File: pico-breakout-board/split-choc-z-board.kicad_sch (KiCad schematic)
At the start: 79 parts, among them J1 USB4105-GF-A, J2 USB4105-GF-A, J3 Conn_01x04_Pin, J4 Conn_01x02, SW1 SW_SPST, SW10 SW_SPST, SW11 SW_SPST, SW12 SW_SPST, SW13 SW_SPST, SW14 SW_SPST, SW15 SW_SPST, SW16 SW_SPST, SW17 SW_SPST, SW18 SW_SPST, SW19 SW_SPST, SW2 SW_SPST, SW20 SW_SPST, SW21 SW_SPST, SW22 SW_SPST, SW3 SW_SPST, SW4 SW_SPST, SW5 SW_SPST, SW6 SW_SPST, SW7 SW_SPST, SW8 SW_SPST, SW9 SW_SPST, U2 RP2040, U3 NCP1117-3.3_SOT223, U4 W25Q128JVS, U5 USBLC6-2SC6, X1 ABM8-272-T3

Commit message: Removed matrix and added 2.54mm pins 2x20
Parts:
- removed D1, D10, D11, D12, D13, D14, D15, D16, D17, D18, D19, D2, D20, D3, D4, D5, D6, D7, D8, D9: D, footprints:SOD123_MCC, symbol Device:D
- removed GND1, GP24, GP25: TestPoint, TestPoint:TestPoint_Pad_D2.0mm, symbol Connector:TestPoint
- removed J4: Conn_01x02, Connector_PinHeader_2.54mm:PinHeader_1x02_P2.54mm_Vertical, symbol Connector_Generic:Conn_01x02
- removed SW1, SW10, SW11, SW12, SW13, SW14, SW15, SW16, SW17, SW18, SW19, SW2, SW20, SW3, SW4, SW5, SW6, SW7, SW8, SW9: SW_SPST, ScottoKeebs_Choc:Choc_V1_1.00u, symbol Switch:SW_SPST
- added J5: Conn_02x20_Counter_Clockwise, Connector_PinHeader_2.54mm:PinHeader_2x20_P2.54mm_Vertical, symbol Connector_Generic:Conn_02x20_Counter_Clockwise
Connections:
- net +3V3: now also J5.25 (Pin_25), J5.26 (Pin_26), J5.27 (Pin_27), J5.28 (Pin_28); no longer U2.2 (GPIO0)
- net B-B_D+: no longer U2.13 (GPIO10)
- net B-B_D-: no longer U2.14 (GPIO11)
- net DEBUG_CLK: now also J5.39 (Pin_39)
- net DEBUG_DATA: now also J5.40 (Pin_40)
- net GND: now also J5.21 (Pin_21), J5.22 (Pin_22), J5.23 (Pin_23), J5.24 (Pin_24)
- net GPIO12: now reaches U2.15 (GPIO12)
- net GPIO12: now also J5.8 (Pin_8)
- net GPIO13: now reaches U2.16 (GPIO13)
- net GPIO13: now also J5.7 (Pin_7)
- net GPIO14: now reaches U2.17 (GPIO14)
- net GPIO14: now also J5.6 (Pin_6)
- net GPIO15: now reaches U2.18 (GPIO15)
- net GPIO15: now also J5.5 (Pin_5)
- net GPIO16: now reaches U2.27 (GPIO16)
- net GPIO16: now also J5.4 (Pin_4)
- net GPIO17: now reaches U2.28 (GPIO17)
- net GPIO17: now also J5.3 (Pin_3)
- net GPIO18: now reaches U2.29 (GPIO18)
- net GPIO18: now also J5.2 (Pin_2)
- net GPIO19: now reaches U2.30 (GPIO19)
- net GPIO19: now also J5.1 (Pin_1)
- net GPIO20: now reaches U2.31 (GPIO20)
- net GPIO20: now also J5.38 (Pin_38)
- net GPIO21: now reaches U2.32 (GPIO21)
- net GPIO21: now also J5.37 (Pin_37)
- net GPIO22: now reaches U2.34 (GPIO22)
- net GPIO22: now also J5.36 (Pin_36)
- net GPIO23: now reaches U2.35 (GPIO23)
- net GPIO23: now also J5.35 (Pin_35)
- net GPIO26: now reaches U2.38 (GPIO26_ADC0)
- net GPIO26: now also J5.32 (Pin_32)
- net GPIO27: now reaches U2.39 (GPIO27_ADC1)
- net GPIO27: now also J5.31 (Pin_31)
- net GPIO28: now reaches U2.40 (GPIO28_ADC2)
- net GPIO28: now also J5.30 (Pin_30)
- net GPIO29: now reaches U2.41 (GPIO29_ADC3)
- net GPIO29: now also J5.29 (Pin_29)
- net Col_1 renamed GPIO1
- net GPIO1: now also J5.19 (Pin_19)
- net Col_2 renamed GPIO2
- net GPIO2: now also J5.18 (Pin_18)
- net Col_3 renamed GPIO3
- net GPIO3: now also J5.17 (Pin_17)
- net Col_4 renamed GPIO4
- net GPIO4: now also J5.16 (Pin_16)
- net GP24 renamed GPIO24
- net GPIO24: now also J5.34 (Pin_34)
- net GP25 renamed GPIO25
- net GPIO25: now also J5.33 (Pin_33)
- net Row_1 renamed GPIO5
- net GPIO5: now also J5.15 (Pin_15)
- net Row_2 renamed GPIO6
- net GPIO6: now also J5.14 (Pin_14)
- net Row_3 renamed GPIO7
- net GPIO7: now also J5.13 (Pin_13)
- net Row_4 renamed GPIO8
- net GPIO8: now also J5.12 (Pin_12)
- net Row_5 renamed GPIO9
- net GPIO9: now also J5.11 (Pin_11)
- new net GPIO0: J5.20 (Pin_20), U2.2 (GPIO0)
- new net GPIO10: J5.10 (Pin_10), U2.13 (GPIO10)
- new net GPIO11: J5.9 (Pin_9), U2.14 (GPIO11)
- no-connect marks 28 -> 12
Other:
- note removed: "Debug"
- note removed: "Keyboard matrix"
- note removed: "Use this in QMK: #define SPLIT_HAND_PIN A0 HIGH is left hand"

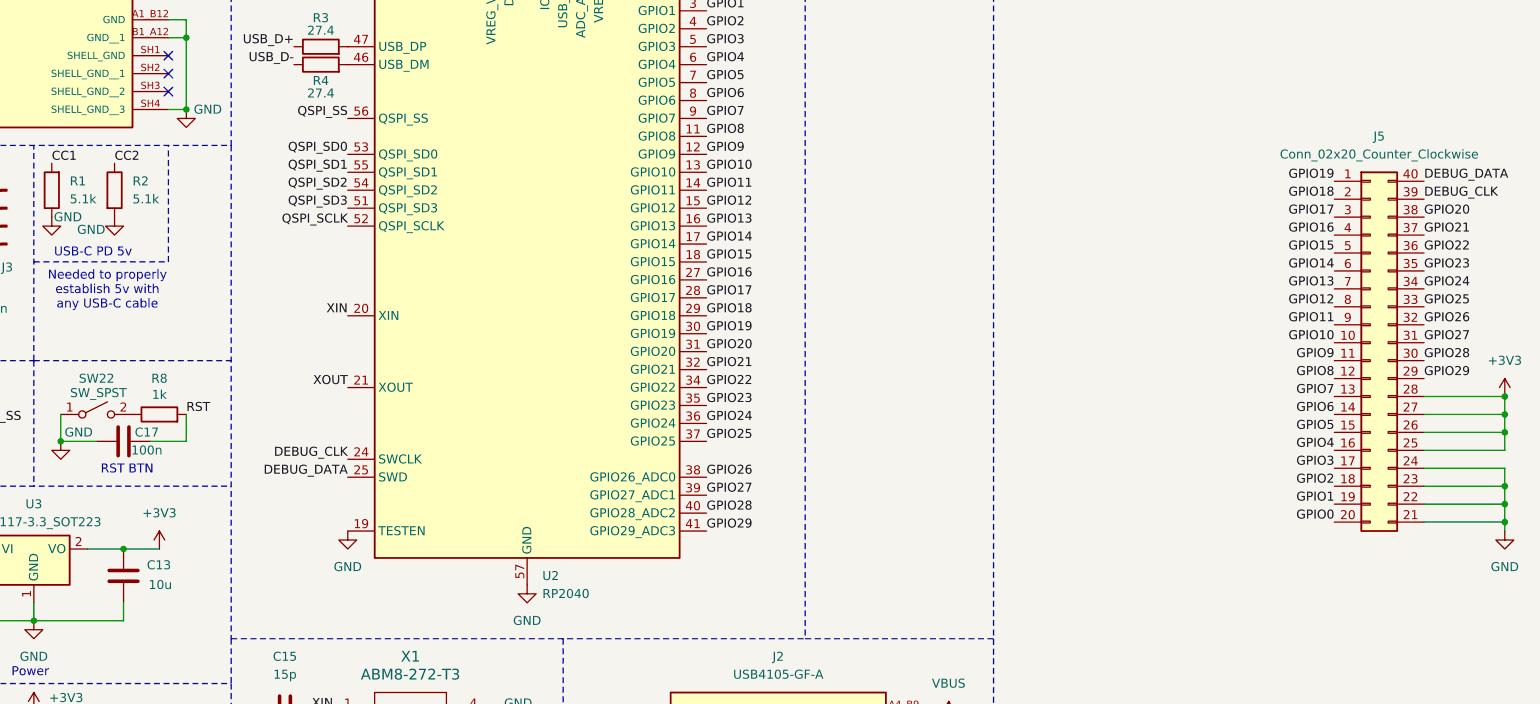
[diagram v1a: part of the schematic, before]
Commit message: Finished bare redesign
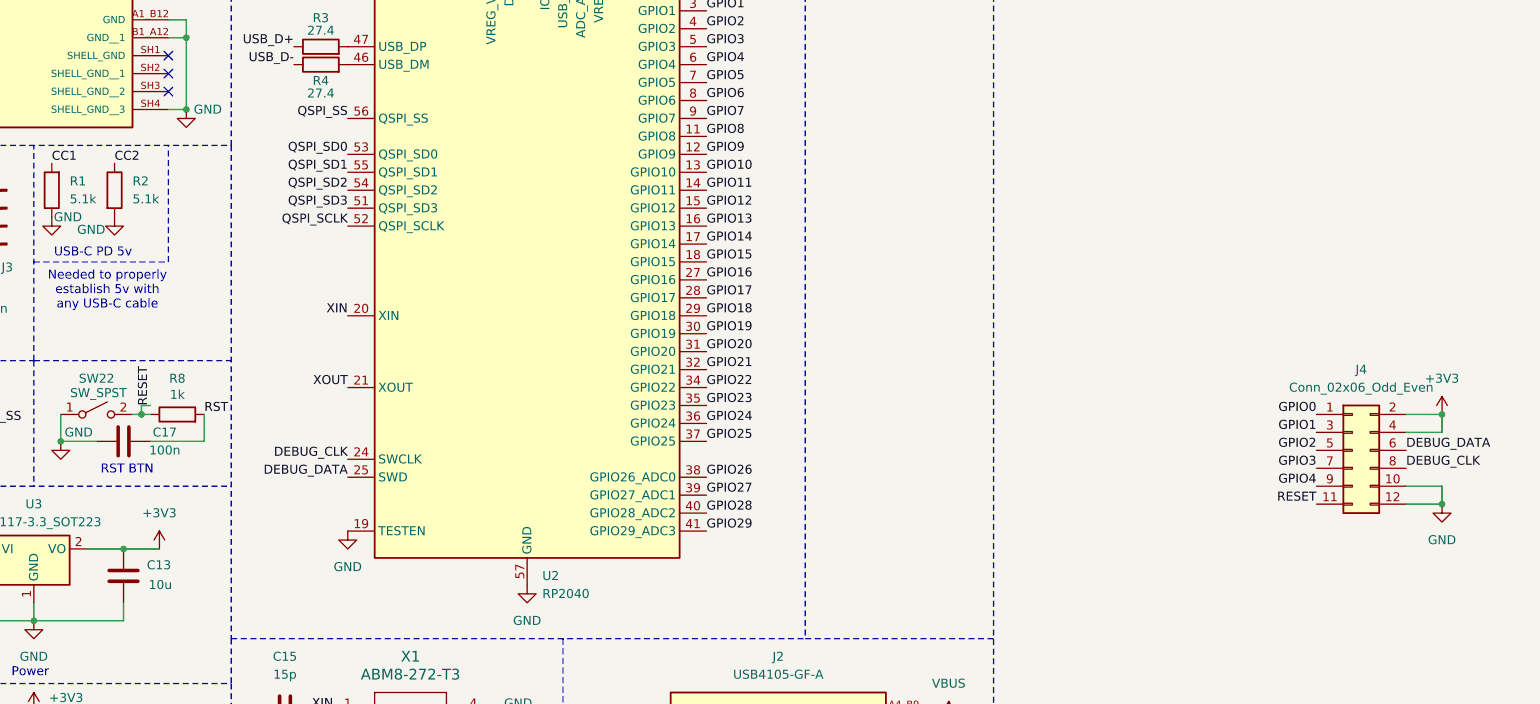
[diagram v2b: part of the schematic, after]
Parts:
- removed J5: Conn_02x20_Counter_Clockwise, Connector_PinHeader_2.54mm:PinHeader_2x20_P2.54mm_Vertical, symbol Connector_Generic:Conn_02x20_Counter_Clockwise
- added J4: Conn_02x06_Odd_Even, Connector_PinSocket_2.54mm:PinSocket_2x06_P2.54mm_Vertical, symbol Connector_Generic:Conn_02x06_Odd_Even
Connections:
- net +3V3: now also J4.2 (Pin_2), J4.4 (Pin_4)
- net DEBUG_CLK: now also J4.8 (Pin_8)
- net DEBUG_DATA: now also J4.6 (Pin_6)
- net GND: now also J4.10 (Pin_10), J4.12 (Pin_12)
- net GPIO0: now also J4.1 (Pin_1)
- net GPIO1: now also J4.3 (Pin_3)
- net GPIO2: now also J4.5 (Pin_5)
- net GPIO3: now also J4.7 (Pin_7)
- net GPIO4: now also J4.9 (Pin_9)
- net RESET: now reaches R8.1, SW22.2 (B)
- net RESET: now also J4.11 (Pin_11)
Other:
- moved on the sheet: R8

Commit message: Forgot no connects
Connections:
- net GPIO10 is gone; now on net B-B_D+: U2.13 (GPIO10)
- net GPIO11 is gone; now on net B-B_D-: U2.14 (GPIO11)
- net GPIO12: no longer names the net of U2.15 (GPIO12)
- net GPIO13: no longer names the net of U2.16 (GPIO13)
- net GPIO14: no longer names the net of U2.17 (GPIO14)
- net GPIO15: no longer names the net of U2.18 (GPIO15)
- net GPIO16: no longer names the net of U2.27 (GPIO16)
- net GPIO17: no longer names the net of U2.28 (GPIO17)
- net GPIO18: no longer names the net of U2.29 (GPIO18)
- net GPIO19: no longer names the net of U2.30 (GPIO19)
- net GPIO20: no longer names the net of U2.31 (GPIO20)
- net GPIO21: no longer names the net of U2.32 (GPIO21)
- net GPIO22: no longer names the net of U2.34 (GPIO22)
- net GPIO23: no longer names the net of U2.35 (GPIO23)
- net GPIO24: no longer names the net of U2.36 (GPIO24)
- net GPIO25: no longer names the net of U2.37 (GPIO25)
- net GPIO26: no longer names the net of U2.38 (GPIO26_ADC0)
- net GPIO27: no longer names the net of U2.39 (GPIO27_ADC1)
- net GPIO28: no longer names the net of U2.40 (GPIO28_ADC2)
- net GPIO29: no longer names the net of U2.41 (GPIO29_ADC3)
- net GPIO5: no longer names the net of U2.7 (GPIO5)
- net GPIO6: no longer names the net of U2.8 (GPIO6)
- net GPIO7: no longer names the net of U2.9 (GPIO7)
- net GPIO8: no longer names the net of U2.11 (GPIO8)
- net GPIO9: no longer names the net of U2.12 (GPIO9)
- no-connect marks 12 -> 35
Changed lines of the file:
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@@
+	)
+	(no_connect
+		(at 137.16 111.76)
+	)
+	(no_connect
+		(at 137.16 60.96)
+	)
+	(no_connect
+		(at 137.16 101.6)
+	)
+	(no_connect
+		(at 137.16 91.44)
 	)
 	(no_connect
@@
 	)
 	(no_connect
+		(at 137.16 83.82)
+	)
+	(no_connect
+		(at 137.16 99.06)
+	)
+	(no_connect
+		(at 137.16 114.3)
+	)
+	(no_connect
+		(at 137.16 78.74)
+	)
+	(no_connect
 		(at 60.96 49.53)
 	)
@@
 	)
 	(no_connect
+		(at 137.16 106.68)
+	)
+	(no_connect
 		(at 167.64 167.64)
 	)
@@
 	)
 	(no_connect
+		(at 137.16 86.36)
+	)
+	(no_connect
 		(at 167.64 170.18)
 	)
@@
 	)
 	(no_connect
+		(at 137.16 93.98)
+	)
+	(no_connect
 		(at 60.96 52.07)
 	)
 	(no_connect
+		(at 137.16 88.9)
+	)
+	(no_connect
+		(at 137.16 81.28)
+	)
+	(no_connect
+		(at 137.16 68.58)
+	)
+	(no_connect
+		(at 137.16 58.42)
+	)
+	(no_connect
+		(at 137.16 55.88)
+	)
+	(no_connect
+		(at 137.16 50.8)
+	)
+	(no_connect
+		(at 137.16 109.22)
+	)
+	(no_connect
+		(at 137.16 71.12)
+	)
+	(no_connect
+		(at 137.16 53.34)
+	)
+	(no_connect
+		(at 137.16 96.52)
+	)
+	(no_connect
+		(at 137.16 76.2)
+	)
+	(no_connect
 		(at 127 144.78)
 	)
@@
 	(no_connect
 		(at 167.64 154.94)
+	)
+	(no_connect
+		(at 137.16 73.66)
 	)
 	(wire
@@
 		)
 	)
-	(label "GPIO12"
-		(at 137.16 68.58 0)
+	(label "B-B_D+"
+		(at 137.16 63.5 0)
+		(effects
+			(font
+				(size 1.27 1.27)
+			)
+			(justify left bottom)
+		)
+	)
+	(label "B-B_D-"
+		(at 137.16 66.04 0)
 		(effects
 			(font
@@
 		)
 	)
-	(label "GPIO23"
-		(at 137.16 96.52 0)
-		(effects
-			(font
-				(size 1.27 1.27)
-			)
-			(justify left bottom)
-		)
-	)
 	(label "DEBUG_CLK"
 		(at 86.36 104.14 180)
@@
 		)
 	)
-	(label "GPIO6"
-		(at 137.16 53.34 0)
-		(effects
-			(font
-				(size 1.27 1.27)
-			)
-			(justify left bottom)
-		)
-	)
 	(label "GPIO1"
 		(at 137.16 40.64 0)
@@
 		)
 	)
-	(label "GPIO17"
-		(at 137.16 81.28 0)
-		(effects
-			(font
-				(size 1.27 1.27)
-			)
-			(justify left bottom)
-		)
-	)
 	(label "QSPI_SD1"
 		(at 31.75 154.94 180)
@@
 		)
 	)
-	(label "GPIO7"
-		(at 137.16 55.88 0)
-		(effects
-			(font
-				(size 1.27 1.27)
-			)
-			(justify left bottom)
-		)
-	)
 	(label "USB_D+"
 		(at 20.32 29.21 180)
@@
 		)
 	)
-	(label "GPIO25"
-		(at 137.16 101.6 0)
-		(effects
-			(font
-				(size 1.27 1.27)
-			)
-			(justify left bottom)
-		)
-	)
 	(label "USB_D-"
 		(at 20.32 31.75 180)
@@
 		)
 	)
-	(label "GPIO24"
-		(at 137.16 99.06 0)
-		(effects
-			(font
-				(size 1.27 1.27)
-			)
-			(justify left bottom)
-		)
-	)
-	(label "GPIO11"
-		(at 137.16 66.04 0)
-		(effects
-			(font
-				(size 1.27 1.27)
-			)
-			(justify left bottom)
-		)
-	)
-	(label "GPIO28"
-		(at 137.16 111.76 0)
-		(effects
-			(font
-				(size 1.27 1.27)
-			)
-			(justify left bottom)
-		)
-	)
 	(label "RESET"
 		(at 58.42 96.52 90)
@@
 		)
 	)
-	(label "GPIO8"
-		(at 137.16 58.42 0)
-		(effects
-			(font
-				(size 1.27 1.27)
-			)
-			(justify left bottom)
-		)
-	)
-	(label "GPIO14"
-		(at 137.16 73.66 0)
-		(effects
-			(font
-				(size 1.27 1.27)
-			)
-			(justify left bottom)
-		)
-	)
 	(label "GPIO3"
 		(at 223.52 105.41 180)
@@
 		)
 	)
-	(label "GPIO9"
-		(at 137.16 60.96 0)
-		(effects
-			(font
-				(size 1.27 1.27)
-			)
-			(justify left bottom)
-		)
-	)
 	(label "B-B_D-"
 		(at 127 149.86 180)
@@
 		)
 	)
-	(label "GPIO13"
-		(at 137.16 71.12 0)
-		(effects
-			(font
-				(size 1.27 1.27)
-			)
-			(justify left bottom)
-		)
-	)
 	(label "QSPI_SD1"
 		(at 86.36 63.5 180)
@@
 		)
 	)
-	(label "GPIO22"
-		(at 137.16 93.98 0)
-		(effects
-			(font
-				(size 1.27 1.27)
-			)
-			(justify left bottom)
-		)
-	)
 	(label "QSPI_SCLK"
 		(at 86.36 71.12 180)
@@
 		)
 	)
-	(label "GPIO18"
-		(at 137.16 83.82 0)
-		(effects
-			(font
-				(size 1.27 1.27)
-			)
-			(justify left bottom)
-		)
-	)
 	(label "DEBUG_CLK"
 		(at 236.22 105.41 0)
@@
 		)
 	)
-	(label "GPIO20"
-		(at 137.16 88.9 0)
-		(effects
-			(font
-				(size 1.27 1.27)
-			)
-			(justify left bottom)
-		)
-	)
 	(label "QSPI_SS"
 		(at 33.02 99.06 0)
@@
 		)
 	)
-	(label "GPIO21"
-		(at 137.16 91.44 0)
-		(effects
-			(font
-				(size 1.27 1.27)
-			)
-			(justify left bottom)
-		)
-	)
 	(label "DEBUG_CLK"
 		(at 31.75 66.04 180)
@@
 		)
 	)
-	(label "GPIO27"
-		(at 137.16 109.22 0)
-		(effects
-			(font
-				(size 1.27 1.27)
-			)
-			(justify left bottom)
-		)
-	)
 	(label "B-B_D+"
 		(at 107.95 168.91 270)
@@
 		)
 	)
-	(label "GPIO5"
-		(at 137.16 50.8 0)
-		(effects
-			(font
-				(size 1.27 1.27)
-			)
-			(justify left bottom)
-		)
-	)
-	(label "GPIO10"
-		(at 137.16 63.5 0)
-		(effects
-			(font
-				(size 1.27 1.27)
-			)
-			(justify left bottom)
-		)
-	)
-	(label "GPIO19"
-		(at 137.16 86.36 0)
-		(effects
-			(font
-				(size 1.27 1.27)
-			)
-			(justify left bottom)
-		)
-	)
-	(label "GPIO15"
-		(at 137.16 76.2 0)
-		(effects
-			(font
-				(size 1.27 1.27)
-			)
-			(justify left bottom)
-		)
-	)
-	(label "GPIO29"
-		(at 137.16 114.3 0)
-		(effects
-			(font
-				(size 1.27 1.27)
-			)
-			(justify left bottom)
-		)
-	)
 	(label "B-B_D-"
 		(at 110.49 172.72 270)
@@
 		(effects
 			(font
-				(size 1.27 1.27)
-			)
-			(justify left bottom)
-		)
-	)
-	(label "GPIO26"
-		(at 137.16 106.68 0)
-		(effects
-			(font
-				(size 1.27 1.27)
-			)
-			(justify left bottom)
-		)
-	)
-	(label "GPIO16"
-		(at 137.16 78.74 0)
-		(effects
-			(font
